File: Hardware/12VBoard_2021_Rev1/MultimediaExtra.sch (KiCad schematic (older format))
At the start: 27 parts

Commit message: current sense
started current sense circuit on hig current. added fuse and LED signal. started tiva wiring.
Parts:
- added C?: CP1, symbol Device:CP1
- added C?: C, symbol Device:C
- added D? (x2): LED, symbol Device:LED
- added F?: Fuse, symbol Device:Fuse
- added Q?: NTR2101P, Package_TO_SOT_SMD:SOT-23, symbol Transistor_FET:NTR2101P
- added R?: 0.01, symbol Device:R
- added R?: 5.1K, symbol Device:R
- added R? (x2): 1k, symbol Device:R
- added R?: R, symbol Device:R
- added SW?: SW_SPDT, symbol Switch:SW_SPDT
- added U?: LT1910, symbol MRDT_ICs:LT1910
- added U?: INA198, Package_TO_SOT_SMD:SOT-23-5, symbol Amplifier_Current:INA198
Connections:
- net labels added: +5V, PackVoltage
- net labels removed: +12V
- wire segments 72 -> 134
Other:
- note added: "Green"

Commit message: current sense
finished adding current sensing to high current side, also started thinking about tiva pin connector layout
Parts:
- R?: value R -> 5m
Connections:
- net labels added: 5V
- net labels removed: +5V
- wire segments 134 -> 137
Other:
- moved on the sheet: C?, D?, F?, Q?, R?, SW?, U?

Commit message: High current
Fisnished adding labes/tags
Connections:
- net 12V15AMultimedia: now reaches C?.1, D?.2 (A), F?.1, R?.2, U?.8 (V+)
- net 12V15AExtra: now reaches D?.2 (A), Q?.2 (S)
- net MultimediaExtraSense: now reaches U?.1
- net CTL1 renamed CTL_AuxMount
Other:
- moved on the sheet: D?, R?
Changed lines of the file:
@@
 $Descr A4 11693 8268
 encoding utf-8
-Sheet 8 8
+Sheet 7 8
 Title ""
 Date ""
@@
 	1    0    0    -1
 $EndComp
-Text GLabel 3150 1700 0    50   Input ~ 0
-CTL1
 $Comp
 L pspice:CAP C?
@@
 U 1 1 5F8CAF09
 P 6050 4600
-F 0 "C?" H 6165 4646 50  0000 L CNN
-F 1 "CP1" H 6165 4555 50  0000 L CNN
+F 0 "C?" H 5900 4500 50  0000 L CNN
+F 1 "CP1" H 5900 4400 50  0000 L CNN
 F 2 "" H 6050 4600 50  0001 C CNN
 F 3 "~" H 6050 4600 50  0001 C CNN
@@
 L Device:R R?
 U 1 1 5F945D14
-P 6550 4250
+P 6300 4250
 AR Path="/5F74F36B/5F821EB2/5F945D14" Ref="R?"  Part="1"
 AR Path="/5F74F36B/5F8236F9/5F945D14" Ref="R?"  Part="1"
-F 0 "R?" H 6620 4296 50  0000 L CNN
-F 1 "1k" H 6620 4205 50  0000 L CNN
-F 2 "" V 6480 4250 50  0001 C CNN
-F 3 "~" H 6550 4250 50  0001 C CNN
-	1    6550 4250
+F 0 "R?" H 6370 4296 50  0000 L CNN
+F 1 "1k" H 6370 4205 50  0000 L CNN
+F 2 "" V 6230 4250 50  0001 C CNN
+F 3 "~" H 6300 4250 50  0001 C CNN
+	1    6300 4250
 	1    0    0    -1
 $EndComp
@@
 L power:GND #PWR?
 U 1 1 5F945D1A
-P 6550 4500
+P 6300 4500
 AR Path="/5F74F36B/5F821EB2/5F945D1A" Ref="#PWR?"  Part="1"
 AR Path="/5F74F36B/5F8236F9/5F945D1A" Ref="#PWR?"  Part="1"
-F 0 "#PWR?" H 6550 4250 50  0001 C CNN
-F 1 "GND" H 6555 4327 50  0000 C CNN
-F 2 "" H 6550 4500 50  0001 C CNN
-F 3 "" H 6550 4500 50  0001 C CNN
-	1    6550 4500
+F 0 "#PWR?" H 6300 4250 50  0001 C CNN
+F 1 "GND" H 6305 4327 50  0000 C CNN
+F 2 "" H 6300 4500 50  0001 C CNN
+F 3 "" H 6300 4500 50  0001 C CNN
+	1    6300 4500
 	1    0    0    -1
 $EndComp
@@
 L Device:LED D?
 U 1 1 5F945D20
-P 6550 3850
+P 6300 3850
 AR Path="/5F74F36B/5F821EB2/5F945D20" Ref="D?"  Part="1"
 AR Path="/5F74F36B/5F8236F9/5F945D20" Ref="D?"  Part="1"
-F 0 "D?" V 6589 3733 50  0000 R CNN
-F 1 "LED" V 6498 3733 50  0000 R CNN
-F 2 "" H 6550 3850 50  0001 C CNN
-F 3 "~" H 6550 3850 50  0001 C CNN
-	1    6550 3850
+F 0 "D?" V 6339 3733 50  0000 R CNN
+F 1 "LED" V 6248 3733 50  0000 R CNN
+F 2 "" H 6300 3850 50  0001 C CNN
+F 3 "~" H 6300 3850 50  0001 C CNN
+	1    6300 3850
 	0    -1   -1   0
 $EndComp
 Wire Wire Line
-	6550 4500 6550 4400
-Wire Wire Line
-	6550 4100 6550 4000
-Wire Wire Line
-	6550 3700 6550 3650
-Wire Wire Line
-	5800 3650 6550 3650
-Wire Wire Line
-	6550 3650 6600 3650
-Connection ~ 6550 3650
+	6300 4500 6300 4400
+Wire Wire Line
+	6300 4100 6300 4000
+Wire Wire Line
+	6300 3700 6300 3650
+Wire Wire Line
+	5800 3650 6300 3650
 $Comp
 L Device:R R?
@@
 	6950 3150 7000 3150
 Connection ~ 6950 3150
-Text Notes 6600 3750 0    50   ~ 0
+Text Notes 6350 3750 0    50   ~ 0
 Green
 Text Notes 7000 3250 0    50   ~ 0
@@
 	4350 3150 3450 3150
 Connection ~ 3450 3150
-Text GLabel 2950 3800 0    50   Input ~ 0
-5V
-Text GLabel 3950 4450 0    50   Input ~ 0
-5V
-Text GLabel 4500 4050 1    50   Input ~ 0
-5V
 Wire Wire Line
 	3000 3800 2950 3800
@@
 	0    1    1    0
 $EndComp
+Text HLabel 2950 3800 0    50   Output ~ 0
+5V
+Text HLabel 3950 4450 0    50   Output ~ 0
+5V
+Text HLabel 4450 4050 0    50   Output ~ 0
+5V
+Wire Wire Line
+	4500 4050 4450 4050
+Text HLabel 6350 3650 2    50   Input ~ 0
+12V15AExtra
+Text HLabel 7000 3150 2    50   Input ~ 0
+12V15AMultimedia
+Wire Wire Line
+	6350 3650 6300 3650
+Connection ~ 6300 3650
+Text HLabel 3250 4250 0    49   Output ~ 0
+MultimediaExtraSense
+Wire Wire Line
+	3300 4200 3300 4250
+Wire Wire Line
+	3300 4250 3250 4250
+Text HLabel 3150 1700 0    49   Input ~ 0
+CTL_AuxMount
 $EndSCHEMATC

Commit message: Added Testpoints
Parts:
- added TP? (x2): TestPoint, symbol Connector:TestPoint
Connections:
- net CTL_AuxMount: now also TP?.1
- net MultimediaExtraSense: now also TP?.1
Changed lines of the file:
@@
 $EndComp
-Wire Wire Line
-	3150 1700 3250 1700
 Wire Wire Line
 	3250 1800 3150 1800
@@
 Wire Wire Line
 	3300 4250 3250 4250
-Text HLabel 3150 1700 0    49   Input ~ 0
+Text HLabel 2850 1700 0    49   Input ~ 0
 CTL_AuxMount
+Wire Wire Line
+	2850 1700 3050 1700
+$Comp
+L Connector:TestPoint TP?
+U 1 1 5F8C03AE
+P 3050 1750
+F 0 "TP?" H 3250 1800 50  0000 R CNN
+F 1 "TestPoint" H 3250 1650 50  0000 R CNN
+F 2 "" H 3250 1750 50  0001 C CNN
+F 3 "~" H 3250 1750 50  0001 C CNN
+	1    3050 1750
+	-1   0    0    1
+$EndComp
+Wire Wire Line
+	3050 1750 3050 1700
+Connection ~ 3050 1700
+Wire Wire Line
+	3050 1700 3250 1700
+$Comp
+L Connector:TestPoint TP?
+U 1 1 5F8CA23D
+P 3350 4250
+F 0 "TP?" V 3450 4350 50  0000 R CNN
+F 1 "TestPoint" V 3550 4450 50  0000 R CNN
+F 2 "" H 3550 4250 50  0001 C CNN
+F 3 "~" H 3550 4250 50  0001 C CNN
+	1    3350 4250
+	0    1    1    0
+$EndComp
+Wire Wire Line
+	3350 4250 3300 4250
+Connection ~ 3300 4250
 $EndSCHEMATC

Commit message: reviewed
review
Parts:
- R? (x2): value 1k -> 1.2k
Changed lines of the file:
@@
 $Descr A4 11693 8268
 encoding utf-8
-Sheet 7 8
+Sheet 6 7
 Title ""
 Date ""
@@
 AR Path="/5F74F36B/5F8236F9/5F945D14" Ref="R?"  Part="1"
 F 0 "R?" H 6370 4296 50  0000 L CNN
-F 1 "1k" H 6370 4205 50  0000 L CNN
+F 1 "1.2k" H 6370 4205 50  0000 L CNN
 F 2 "" V 6230 4250 50  0001 C CNN
 F 3 "~" H 6300 4250 50  0001 C CNN
@@
 AR Path="/5F74F36B/5F8236F9/5F955B34" Ref="R?"  Part="1"
 F 0 "R?" H 7020 3796 50  0000 L CNN
-F 1 "1k" H 7020 3705 50  0000 L CNN
+F 1 "1.2k" H 7020 3705 50  0000 L CNN
 F 2 "" V 6880 3750 50  0001 C CNN
 F 3 "~" H 6950 3750 50  0001 C CNN

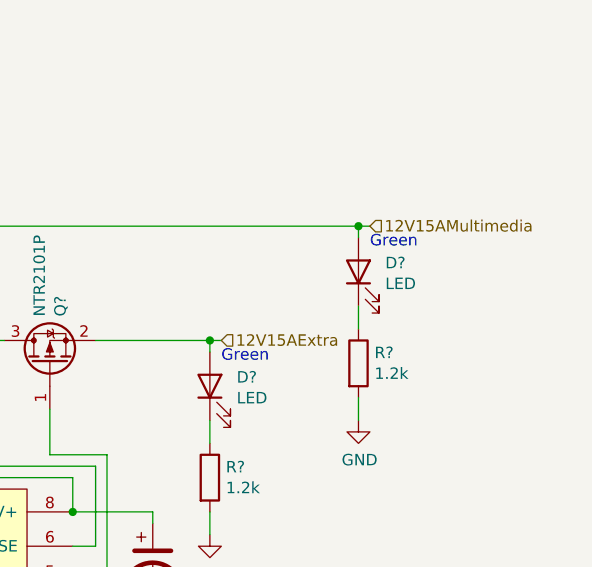
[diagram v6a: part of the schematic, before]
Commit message: fixed High current for second review
addes gimbal to high current. added teva digital write pin to gimbal fot CTL. changed ports from 15 to 10 amp
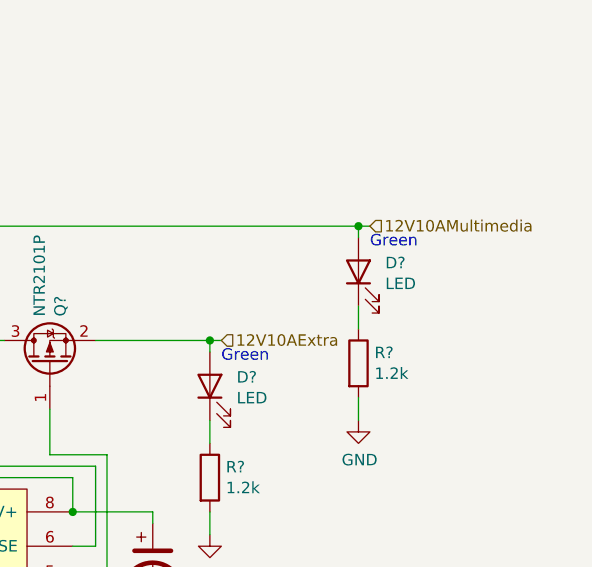
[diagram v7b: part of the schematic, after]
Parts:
- removed C? (x2): 10uF, symbol pspice:CAP
- removed C?: 0.47uF, symbol pspice:CAP
- removed C?: 1uF, symbol pspice:CAP
- removed C?: 0.01uF, symbol pspice:CAP
- removed C?: 220uF, symbol Device:CP1
- removed L?: L, symbol Device:L
- removed R?: R, symbol Device:R
- added C? (x2): 10uF, symbol pspice:CAP
- added C?: 0.47uF, symbol pspice:CAP
- added C?: 1uF, symbol pspice:CAP
- added C?: 0.01uF, symbol pspice:CAP
- added C?: 220uF, symbol Device:CP1
- added L?: L, symbol Device:L
- added R?: R, symbol Device:R
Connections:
- net GND: now also C?.2, C?.2, C?.2, C?.2, C?.2, R?.1
- net NchMID: now also C?.1, L?.2
- net PackVoltage: now also C?.1
- net Vo: now also C?.1, C?.1, L?.1
- net at U?.15 (BST): now also C?.2
- net at U?.20 (REG5): now also C?.1
- net at U?.5 (RCL): now also R?.2
- net at U?.2 (SS): now also C?.1
- net 12V15AExtra renamed 12V10AExtra
- net 12V15AMultimedia renamed 12V10AMultimedia
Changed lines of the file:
@@
 $Descr A4 11693 8268
 encoding utf-8
-Sheet 6 7
+Sheet 6 8
 Title ""
 Date ""
@@
 $Comp
 L pspice:CAP C?
-U 1 1 5F844319
+U 1 1 5F971E20
 P 1900 1050
-AR Path="/5F74F36B/5F844319" Ref="C?"  Part="1"
-AR Path="/5F74F36B/5F8222BE/5F844319" Ref="C?"  Part="1"
-AR Path="/5F74F36B/5F821EB2/5F844319" Ref="C?"  Part="1"
-AR Path="/5F74F36B/5F8236F9/5F844319" Ref="C?"  Part="1"
+AR Path="/5F74F36B/5F971E20" Ref="C?"  Part="1"
+AR Path="/5F74F36B/5F8222BE/5F971E20" Ref="C?"  Part="1"
+AR Path="/5F74F36B/5F821EB2/5F971E20" Ref="C?"  Part="1"
+AR Path="/5F74F36B/5F8236F9/5F971E20" Ref="C?"  Part="1"
 F 0 "C?" H 2078 1096 50  0000 L CNN
 F 1 "10uF" H 2078 1005 50  0000 L CNN
@@
 $Comp
 L pspice:CAP C?
-U 1 1 5F84435D
+U 1 1 5F971E21
 P 3500 850
-AR Path="/5F74F36B/5F84435D" Ref="C?"  Part="1"
-AR Path="/5F74F36B/5F8222BE/5F84435D" Ref="C?"  Part="1"
-AR Path="/5F74F36B/5F821EB2/5F84435D" Ref="C?"  Part="1"
-AR Path="/5F74F36B/5F8236F9/5F84435D" Ref="C?"  Part="1"
+AR Path="/5F74F36B/5F971E21" Ref="C?"  Part="1"
+AR Path="/5F74F36B/5F8222BE/5F971E21" Ref="C?"  Part="1"
+AR Path="/5F74F36B/5F821EB2/5F971E21" Ref="C?"  Part="1"
+AR Path="/5F74F36B/5F8236F9/5F971E21" Ref="C?"  Part="1"
 F 0 "C?" H 3300 950 50  0000 L CNN
 F 1 "0.47uF" H 3200 1050 50  0000 L CNN
@@
 $Comp
 L pspice:CAP C?
-U 1 1 5F844364
+U 1 1 5F971E22
 P 3150 2100
-AR Path="/5F74F36B/5F844364" Ref="C?"  Part="1"
-AR Path="/5F74F36B/5F8222BE/5F844364" Ref="C?"  Part="1"
-AR Path="/5F74F36B/5F821EB2/5F844364" Ref="C?"  Part="1"
-AR Path="/5F74F36B/5F8236F9/5F844364" Ref="C?"  Part="1"
+AR Path="/5F74F36B/5F971E22" Ref="C?"  Part="1"
+AR Path="/5F74F36B/5F8222BE/5F971E22" Ref="C?"  Part="1"
+AR Path="/5F74F36B/5F821EB2/5F971E22" Ref="C?"  Part="1"
+AR Path="/5F74F36B/5F8236F9/5F971E22" Ref="C?"  Part="1"
 F 0 "C?" H 3000 2200 50  0000 L CNN
 F 1 "1uF" H 3000 2000 50  0000 L CNN
@@
 $Comp
 L power:GND #PWR?
-U 1 1 5F84436A
+U 1 1 5F971E23
 P 3150 2400
-AR Path="/5F74F36B/5F84436A" Ref="#PWR?"  Part="1"
-AR Path="/5F74F36B/5F8222BE/5F84436A" Ref="#PWR?"  Part="1"
-AR Path="/5F74F36B/5F821EB2/5F84436A" Ref="#PWR?"  Part="1"
-AR Path="/5F74F36B/5F8236F9/5F84436A" Ref="#PWR?"  Part="1"
+AR Path="/5F74F36B/5F971E23" Ref="#PWR?"  Part="1"
+AR Path="/5F74F36B/5F8222BE/5F971E23" Ref="#PWR?"  Part="1"
+AR Path="/5F74F36B/5F821EB2/5F971E23" Ref="#PWR?"  Part="1"
+AR Path="/5F74F36B/5F8236F9/5F971E23" Ref="#PWR?"  Part="1"
 F 0 "#PWR?" H 3150 2150 50  0001 C CNN
 F 1 "GND" H 3155 2227 50  0000 C CNN
@@
 $Comp
 L power:GND #PWR?
-U 1 1 5F844370
+U 1 1 5F971E24
 P 3600 2000
-AR Path="/5F74F36B/5F844370" Ref="#PWR?"  Part="1"
-AR Path="/5F74F36B/5F8222BE/5F844370" Ref="#PWR?"  Part="1"
-AR Path="/5F74F36B/5F821EB2/5F844370" Ref="#PWR?"  Part="1"
-AR Path="/5F74F36B/5F8236F9/5F844370" Ref="#PWR?"  Part="1"
+AR Path="/5F74F36B/5F971E24" Ref="#PWR?"  Part="1"
+AR Path="/5F74F36B/5F8222BE/5F971E24" Ref="#PWR?"  Part="1"
+AR Path="/5F74F36B/5F821EB2/5F971E24" Ref="#PWR?"  Part="1"
+AR Path="/5F74F36B/5F8236F9/5F971E24" Ref="#PWR?"  Part="1"
 F 0 "#PWR?" H 3600 1750 50  0001 C CNN
 F 1 "GND" H 3500 1900 50  0000 C CNN
@@
 $Comp
 L power:GND #PWR?
-U 1 1 5F844376
+U 1 1 5F971E25
 P 4450 1550
-AR Path="/5F74F36B/5F844376" Ref="#PWR?"  Part="1"
-AR Path="/5F74F36B/5F8222BE/5F844376" Ref="#PWR?"  Part="1"
-AR Path="/5F74F36B/5F821EB2/5F844376" Ref="#PWR?"  Part="1"
-AR Path="/5F74F36B/5F8236F9/5F844376" Ref="#PWR?"  Part="1"
+AR Path="/5F74F36B/5F971E25" Ref="#PWR?"  Part="1"
+AR Path="/5F74F36B/5F8222BE/5F971E25" Ref="#PWR?"  Part="1"
+AR Path="/5F74F36B/5F821EB2/5F971E25" Ref="#PWR?"  Part="1"
+AR Path="/5F74F36B/5F8236F9/5F971E25" Ref="#PWR?"  Part="1"
 F 0 "#PWR?" H 4450 1300 50  0001 C CNN
 F 1 "GND" H 4550 1550 50  0000 C CNN
@@
 $Comp
 L Device:R R?
-U 1 1 5F84437E
+U 1 1 5F971E26
 P 4200 2050
-AR Path="/5F74F36B/5F84437E" Ref="R?"  Part="1"
-AR Path="/5F74F36B/5F8222BE/5F84437E" Ref="R?"  Part="1"
-AR Path="/5F74F36B/5F821EB2/5F84437E" Ref="R?"  Part="1"
-AR Path="/5F74F36B/5F8236F9/5F84437E" Ref="R?"  Part="1"
+AR Path="/5F74F36B/5F971E26" Ref="R?"  Part="1"
+AR Path="/5F74F36B/5F8222BE/5F971E26" Ref="R?"  Part="1"
+AR Path="/5F74F36B/5F821EB2/5F971E26" Ref="R?"  Part="1"
+AR Path="/5F74F36B/5F8236F9/5F971E26" Ref="R?"  Part="1"
 F 0 "R?" V 4300 1950 50  0000 C CNN
 F 1 "R" V 4300 2050 50  0000 C CNN
@@
 $Comp
 L pspice:CAP C?
-U 1 1 5F844384
+U 1 1 5F971E27
 P 3700 2400
-AR Path="/5F74F36B/5F844384" Ref="C?"  Part="1"
-AR Path="/5F74F36B/5F8222BE/5F844384" Ref="C?"  Part="1"
-AR Path="/5F74F36B/5F821EB2/5F844384" Ref="C?"  Part="1"
-AR Path="/5F74F36B/5F8236F9/5F844384" Ref="C?"  Part="1"
+AR Path="/5F74F36B/5F971E27" Ref="C?"  Part="1"
+AR Path="/5F74F36B/5F8222BE/5F971E27" Ref="C?"  Part="1"
+AR Path="/5F74F36B/5F821EB2/5F971E27" Ref="C?"  Part="1"
+AR Path="/5F74F36B/5F8236F9/5F971E27" Ref="C?"  Part="1"
 F 0 "C?" H 3550 2500 50  0000 L CNN
 F 1 "0.01uF" H 3550 2300 50  0000 L CNN
@@
 $Comp
 L power:GND #PWR?
-U 1 1 5F84438A
+U 1 1 5F971E28
 P 3700 2700
-AR Path="/5F74F36B/5F84438A" Ref="#PWR?"  Part="1"
-AR Path="/5F74F36B/5F8222BE/5F84438A" Ref="#PWR?"  Part="1"
-AR Path="/5F74F36B/5F821EB2/5F84438A" Ref="#PWR?"  Part="1"
-AR Path="/5F74F36B/5F8236F9/5F84438A" Ref="#PWR?"  Part="1"
+AR Path="/5F74F36B/5F971E28" Ref="#PWR?"  Part="1"
+AR Path="/5F74F36B/5F8222BE/5F971E28" Ref="#PWR?"  Part="1"
+AR Path="/5F74F36B/5F821EB2/5F971E28" Ref="#PWR?"  Part="1"
+AR Path="/5F74F36B/5F8236F9/5F971E28" Ref="#PWR?"  Part="1"
 F 0 "#PWR?" H 3700 2450 50  0001 C CNN
 F 1 "GND" H 3705 2527 50  0000 C CNN
@@
 $Comp
 L pspice:CAP C?
-U 1 1 5F84440C
+U 1 1 5F971E30
 P 1050 3400
-AR Path="/5F74F36B/5F84440C" Ref="C?"  Part="1"
-AR Path="/5F74F36B/5F8222BE/5F84440C" Ref="C?"  Part="1"
-AR Path="/5F74F36B/5F821EB2/5F84440C" Ref="C?"  Part="1"
-AR Path="/5F74F36B/5F8236F9/5F84440C" Ref="C?"  Part="1"
+AR Path="/5F74F36B/5F971E30" Ref="C?"  Part="1"
+AR Path="/5F74F36B/5F8222BE/5F971E30" Ref="C?"  Part="1"
+AR Path="/5F74F36B/5F821EB2/5F971E30" Ref="C?"  Part="1"
+AR Path="/5F74F36B/5F8236F9/5F971E30" Ref="C?"  Part="1"
 F 0 "C?" H 1228 3446 50  0000 L CNN
 F 1 "10uF" H 1228 3355 50  0000 L CNN
@@
 $Comp
 L Device:L L?
-U 1 1 5F84442F
+U 1 1 5F971E34
 P 850 3150
-AR Path="/5F74F36B/5F84442F" Ref="L?"  Part="1"
-AR Path="/5F74F36B/5F8222BE/5F84442F" Ref="L?"  Part="1"
-AR Path="/5F74F36B/5F821EB2/5F84442F" Ref="L?"  Part="1"
-AR Path="/5F74F36B/5F8236F9/5F84442F" Ref="L?"  Part="1"
+AR Path="/5F74F36B/5F971E34" Ref="L?"  Part="1"
+AR Path="/5F74F36B/5F8222BE/5F971E34" Ref="L?"  Part="1"
+AR Path="/5F74F36B/5F821EB2/5F971E34" Ref="L?"  Part="1"
+AR Path="/5F74F36B/5F8236F9/5F971E34" Ref="L?"  Part="1"
 F 0 "L?" V 669 3150 50  0000 C CNN
 F 1 "L" V 760 3150 50  0000 C CNN
@@
 $Comp
 L Device:CP1 C?
-U 1 1 5F84443A
+U 1 1 5F971E35
 P 2550 3400
-AR Path="/5F74F36B/5F84443A" Ref="C?"  Part="1"
-AR Path="/5F74F36B/5F8222BE/5F84443A" Ref="C?"  Part="1"
-AR Path="/5F74F36B/5F821EB2/5F84443A" Ref="C?"  Part="1"
-AR Path="/5F74F36B/5F8236F9/5F84443A" Ref="C?"  Part="1"
+AR Path="/5F74F36B/5F971E35" Ref="C?"  Part="1"
+AR Path="/5F74F36B/5F8222BE/5F971E35" Ref="C?"  Part="1"
+AR Path="/5F74F36B/5F821EB2/5F971E35" Ref="C?"  Part="1"
+AR Path="/5F74F36B/5F8236F9/5F971E35" Ref="C?"  Part="1"
 F 0 "C?" H 2665 3446 50  0000 L CNN
 F 1 "220uF" H 2665 3355 50  0000 L CNN
@@
 $Comp
 L power:GND #PWR?
-U 1 1 5F844440
+U 1 1 5F971E36
 P 2550 3600
-AR Path="/5F74F36B/5F844440" Ref="#PWR?"  Part="1"
-AR Path="/5F74F36B/5F8222BE/5F844440" Ref="#PWR?"  Part="1"
-AR Path="/5F74F36B/5F821EB2/5F844440" Ref="#PWR?"  Part="1"
-AR Path="/5F74F36B/5F8236F9/5F844440" Ref="#PWR?"  Part="1"
+AR Path="/5F74F36B/5F971E36" Ref="#PWR?"  Part="1"
+AR Path="/5F74F36B/5F8222BE/5F971E36" Ref="#PWR?"  Part="1"
+AR Path="/5F74F36B/5F821EB2/5F971E36" Ref="#PWR?"  Part="1"
+AR Path="/5F74F36B/5F8236F9/5F971E36" Ref="#PWR?"  Part="1"
 F 0 "#PWR?" H 2550 3350 50  0001 C CNN
 F 1 "GND" H 2555 3427 50  0000 C CNN
@@
 	4500 4050 4450 4050
 Text HLabel 6350 3650 2    50   Input ~ 0
-12V15AExtra
+12V10AExtra
 Text HLabel 7000 3150 2    50   Input ~ 0
-12V15AMultimedia
+12V10AMultimedia
 Wire Wire Line
 	6350 3650 6300 3650

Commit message: fixed some stuffs
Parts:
- C11, C12, C13, C14, C15, C16, C17, C19, C22: renamed from C?; footprint (none) -> Capacitor_SMD:C_0603_1608Metric_Pad1.05x0.95mm_HandSolder
- D12, D13: renamed from D?; footprint (none) -> Diode_SMD:D_0603_1608Metric_Pad1.05x0.95mm_HandSolder
- F1: renamed from F?; value Fuse -> 10AMP
- R13: renamed from R?; value 5m -> 500m
- R9: renamed from R?; footprint (none) -> Resistor_SMD:R_0603_1608Metric_Pad1.05x0.95mm_HandSolder
- TP5, TP6: renamed from TP?; footprint (none) -> TestPoint:TestPoint_Pad_2.5x2.5mm
- gave numbers to parts that had none: 27
